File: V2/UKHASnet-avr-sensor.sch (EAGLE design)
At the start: 34 parts, among them J1 AVR_SPI_PRG_62X3_LOCK, U1 MCP1700-3302E/TO, U2 ATMEGA328P-PU, X1 SMA-142-0711-881/886, Y1 RESONATORPTH

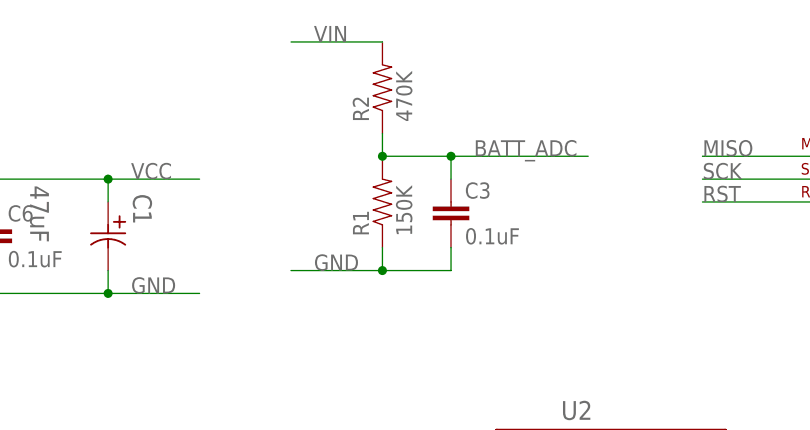
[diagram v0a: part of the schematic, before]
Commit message: V2: Add to BOM.
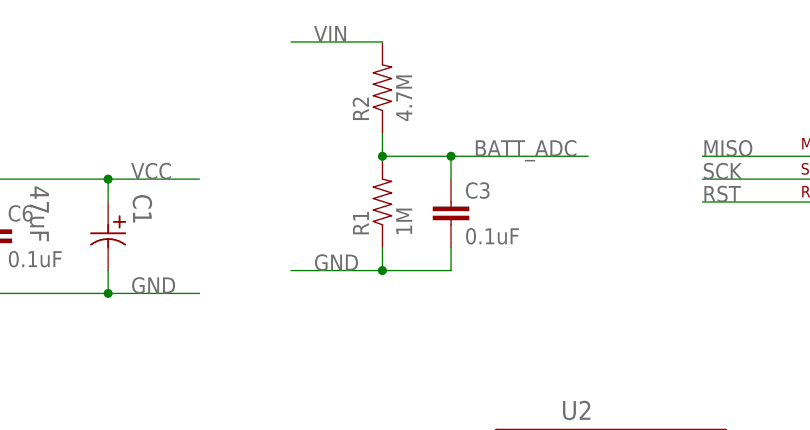
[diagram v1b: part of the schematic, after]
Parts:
- R1: value 150K -> 1M
- R2: value 470K -> 4.7M
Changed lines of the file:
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@@
 <part name="U1" library="mcp1700" deviceset="MCP1700-3302E/TO" device=""/>
 <part name="JP9" library="SparkFun-Connectors" deviceset="M01" device="PTH"/>
-<part name="R1" library="SparkFun" deviceset="RESISTOR" device="PTH-1/4W" value="150K"/>
-<part name="R2" library="SparkFun" deviceset="RESISTOR" device="PTH-1/4W" value="470K"/>
+<part name="R1" library="SparkFun" deviceset="RESISTOR" device="PTH-1/4W" value="1M"/>
+<part name="R2" library="SparkFun" deviceset="RESISTOR" device="PTH-1/4W" value="4.7M"/>
 <part name="R3" library="SparkFun" deviceset="RESISTOR" device="PTH-1/4W" value="10K"/>
 <part name="C1" library="1000ufCap" deviceset="EEU" device="-P1.5" technology="FC1J6R8" value="47uF"/>
